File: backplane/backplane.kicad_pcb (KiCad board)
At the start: 2 copper layers, 150 x 150 mm, 16 parts

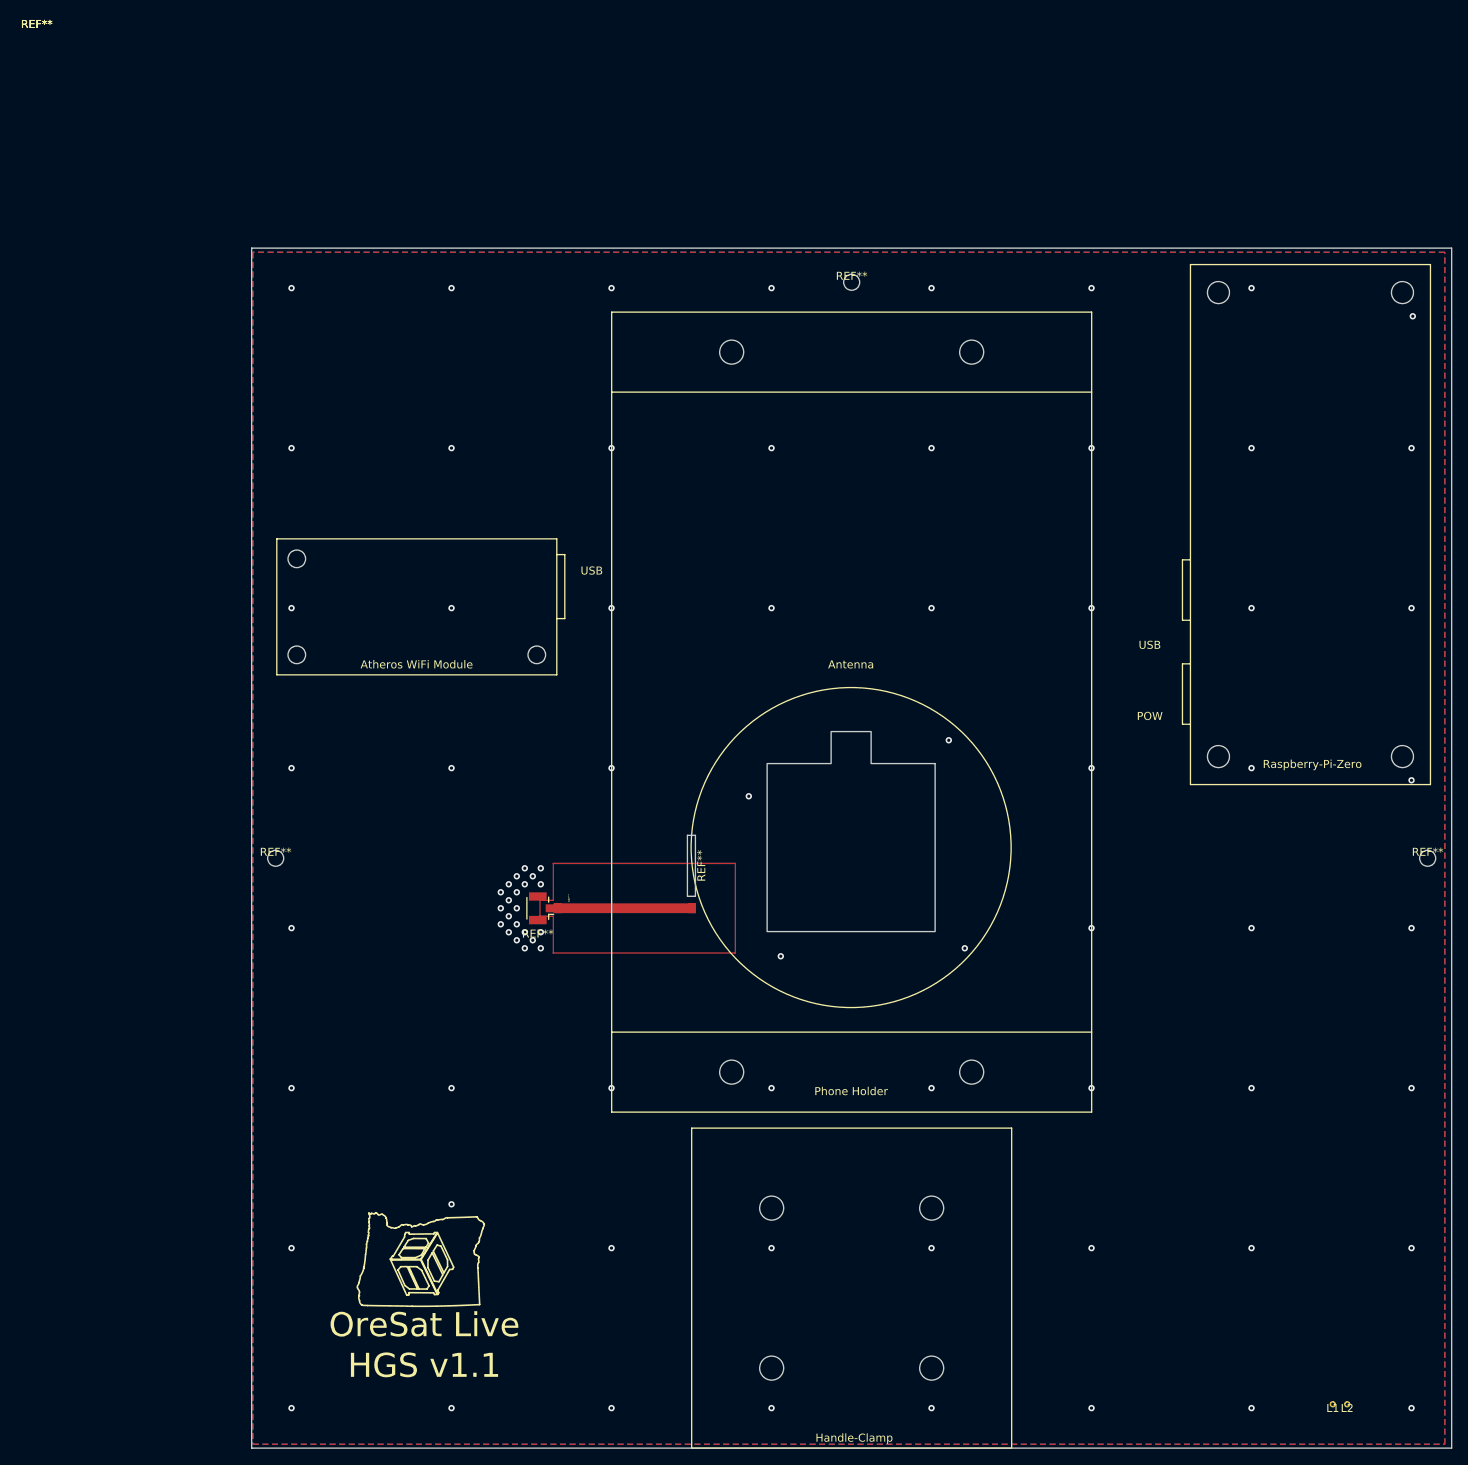
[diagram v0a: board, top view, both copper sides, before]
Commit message: Changed antenna feed slot width to be 1.5mm and other
Cleaned up floating unnecessary silkscreen
Removed solder mask for mounting holes
Updated version number text for HGS
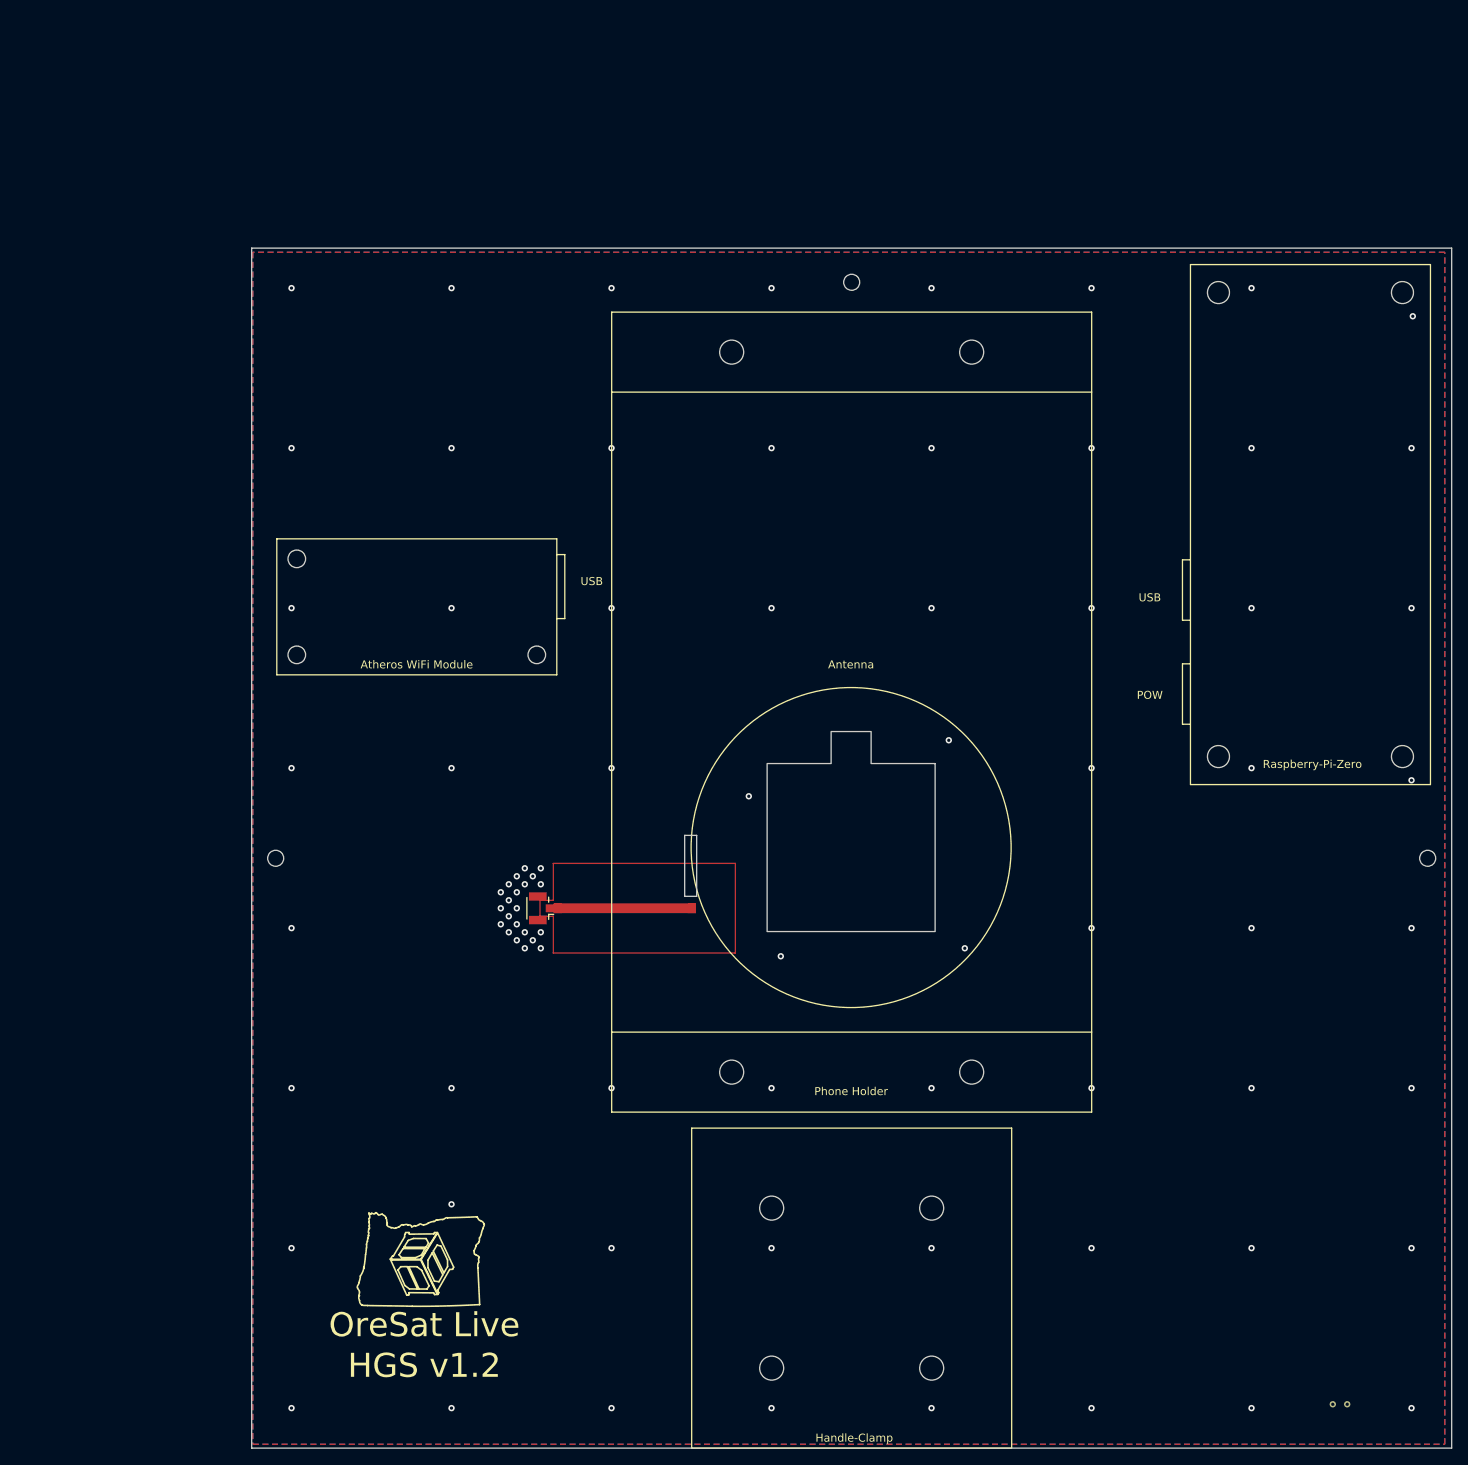
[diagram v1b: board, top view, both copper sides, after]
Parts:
- moved REF** 0.16 mm to (79.8, 107.7)

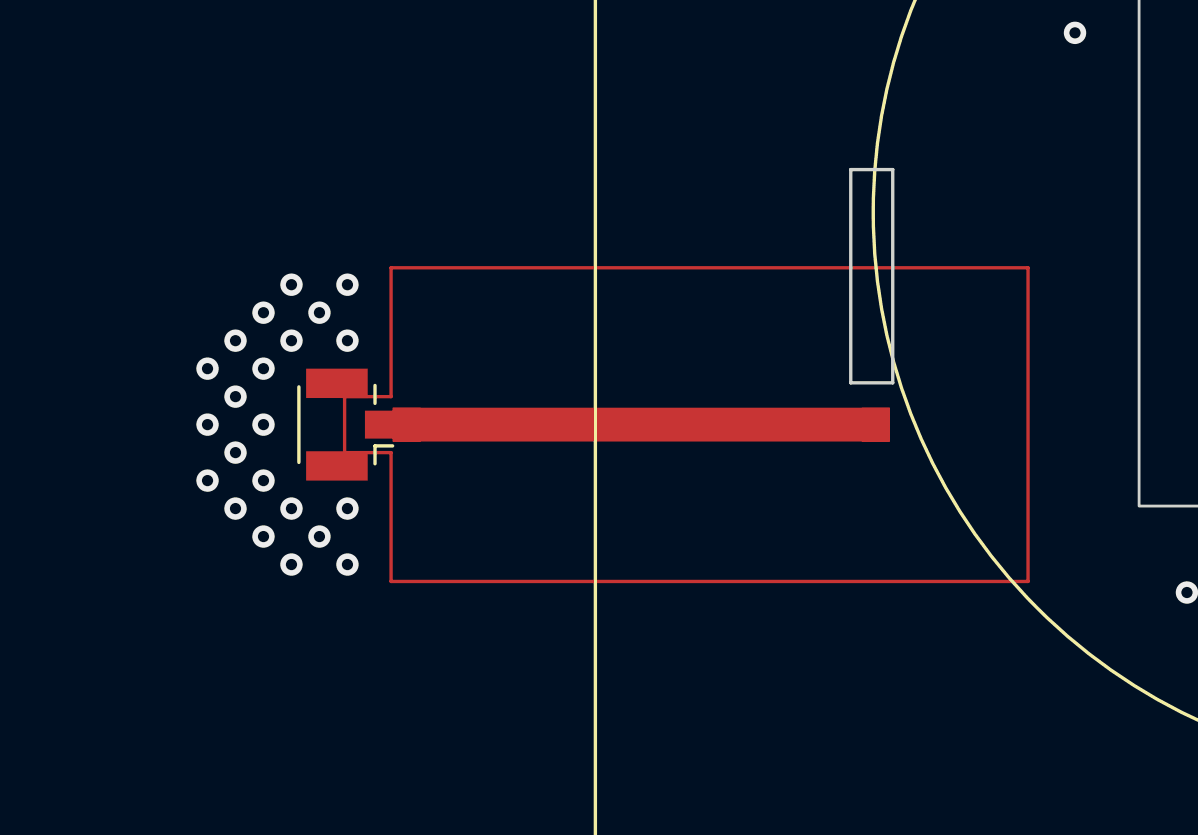
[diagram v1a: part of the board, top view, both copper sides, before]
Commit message: Shifted transformer 1mm to the side and 3mm downward
Transformer was moved so that there is a smoother transition for the
antenna wire to feed to the back of the board.
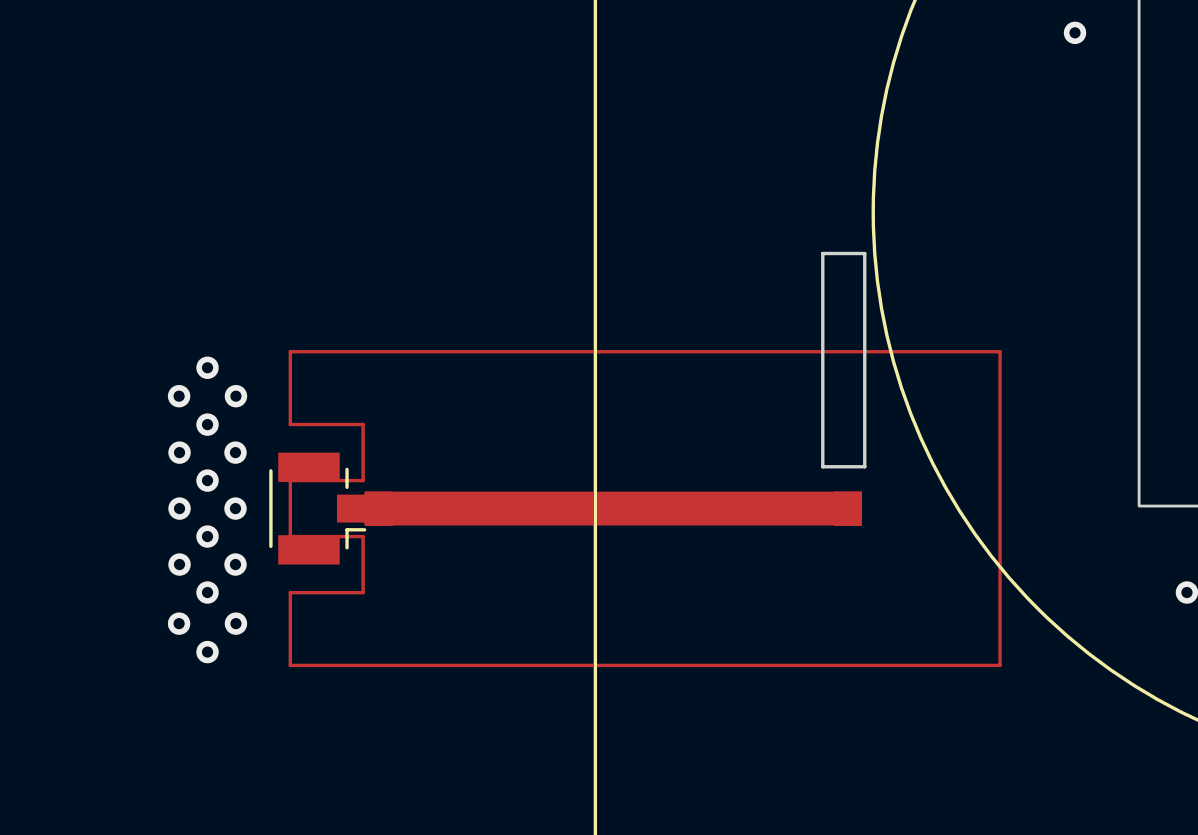
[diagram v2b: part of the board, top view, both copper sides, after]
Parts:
- moved REF** 3.16 mm to (62.0, 116.0)
- moved REF** 3.16 mm to (78.8, 110.7)
- moved REF** 3.16 mm to (58.1, 116.0)
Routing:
- net Net-(L1-Pad1): vias 84 -> 78
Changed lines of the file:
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@@
     (thickness 1.6)
     (drawings 4)
-    (tracks 84)
+    (tracks 78)
     (zones 0)
     (modules 16)
@@
     (add_net "Net-(L1-Pad1)")
   )
+  (module muwave_stub locked (layer F.Cu)
+    (at 62.03385 116 270)
+    (fp_text reference REF** (at -1.27 0.5 90) (layer B.Fab) hide
+      (effects (font (size 0.25 0.25) (thickness 0.05)))
+    )
+    (fp_text value muwave_stub (at 0 -0.5 90) (layer F.Fab)
+      (effects (font (size 0.25 0.25) (thickness 0.05)))
+    )
+    (fp_line (start -3.00469 2.475001) (end -3.00469 5.075001) (layer F.Cu) (width 0.12))
+    (fp_line (start 1 2.475001) (end 1 5.075001) (layer F.Cu) (width 0.12))
+    (fp_line (start -1 5.075001) (end 1 5.075001) (layer F.Cu) (width 0.12))
+    (fp_line (start -5.60469 5.075001) (end -3.00469 5.075001) (layer F.Cu) (width 0.12))
+    (fp_line (start -5.60469 -20.287299) (end 5.60469 -20.287299) (layer F.Cu) (width 0.12))
+    (fp_line (start -5.60469 -20.287299) (end -5.60469 5.075001) (layer F.Cu) (width 0.12))
+    (fp_line (start -1 2.475001) (end -1 5.075001) (layer F.Cu) (width 0.12))
+    (fp_line (start -3.00469 2.475001) (end -1 2.475001) (layer F.Cu) (width 0.12))
+    (fp_line (start 3.00469 2.475001) (end 1 2.475001) (layer F.Cu) (width 0.12))
+    (fp_line (start 5.60469 -20.287299) (end 5.60469 5.075001) (layer F.Cu) (width 0.12))
+    (fp_line (start 5.60469 5.075001) (end 3.00469 5.075001) (layer F.Cu) (width 0.12))
+    (fp_line (start 3.00469 2.475001) (end 3.00469 5.075001) (layer F.Cu) (width 0.12))
+    (pad 1 smd rect (at 0 -6.46615 270) (size 1.20938 17.7623) (layers F.Cu))
+    (pad 1 smd rect (at 0 -14.8473 270) (size 1.20938 1) (layers F.Cu F.Mask))
+    (pad 1 smd rect (at 0 1.915 270) (size 1.20938 1) (layers F.Cu F.Mask))
+  )
   (module DxWiFi:antenna-wire-slot (layer F.Cu)
-    (at 79.756 107.696 270)
+    (at 78.756 110.696 270)
     (fp_text reference REF** (at 0 0.5 270) (layer B.Fab) hide
       (effects (font (size 1 1) (thickness 0.15)))
@@
   )
   (module Connector_Coaxial:U.FL_Hirose_U.FL-R-SMT-1_Vertical (layer F.Cu)
-    (at 59.1 113 180)
+    (at 58.1 116 180)
     (descr "Hirose U.FL Coaxial https://www.hirose.com/product/en/products/U.FL/U.FL-R-SMT-1%2810%29/")
     (tags "Hirose U.FL Coaxial")
@@
     (pad "" np_thru_hole circle (at 10 -10) (size 3 3) (drill 3) (layers *.Cu))
   )
-  (module muwave_stub locked (layer F.Cu)
-    (at 63.03385 113 270)
-    (fp_text reference REF** (at -1.27 0.5 270) (layer B.Fab) hide
-      (effects (font (size 0.25 0.25) (thickness 0.05)))
-    )
-    (fp_text value muwave_stub (at 0 -0.5 270) (layer F.Fab)
-      (effects (font (size 0.25 0.25) (thickness 0.05)))
-    )
-    (fp_line (start -1 2.475001) (end -1 4.135001) (layer F.Cu) (width 0.12))
-    (fp_line (start 1 2.475001) (end 5.60469 2.475001) (layer F.Cu) (width 0.12))
-    (fp_line (start -5.60469 -20.287299) (end -5.60469 2.475001) (layer F.Cu) (width 0.12))
-    (fp_line (start -5.60469 -20.287299) (end 5.60469 -20.287299) (layer F.Cu) (width 0.12))
-    (fp_line (start 5.60469 -20.287299) (end 5.60469 2.475001) (layer F.Cu) (width 0.12))
-    (fp_line (start -5.60469 2.475001) (end -1 2.475001) (layer F.Cu) (width 0.12))
-    (fp_line (start 1 2.475001) (end 1 4.135001) (layer F.Cu) (width 0.12))
-    (fp_line (start -1 4.135001) (end 1 4.135001) (layer F.Cu) (width 0.12))
-    (pad 1 smd rect (at 0 1.915 270) (size 1.20938 1) (layers F.Cu F.Mask))
-    (pad 1 smd rect (at 0 -14.8473 270) (size 1.20938 1) (layers F.Cu F.Mask))
-    (pad 1 smd rect (at 0 -6.46615 270) (size 1.20938 17.7623) (layers F.Cu))
-  )
   (gr_line (start 22.86 180.48) (end 22.86 30.48) (layer Edge.Cuts) (width 0.05))
   (gr_line (start 172.86 180.48) (end 22.86 180.48) (layer Edge.Cuts) (width 0.05))
   (gr_line (start 172.86 30.48) (end 172.86 180.48) (layer Edge.Cuts) (width 0.05))
   (gr_line (start 22.86 30.48) (end 172.86 30.48) (layer Edge.Cuts) (width 0.05))
-  (via (at 59 110) (size 0.8) (drill 0.4) (layers F.Cu B.Cu) (net 1))
-  (via (at 59 108) (size 0.8) (drill 0.4) (layers F.Cu B.Cu) (net 1))
-  (via (at 58 109) (size 0.8) (drill 0.4) (layers F.Cu B.Cu) (net 1))
-  (via (at 57 108) (size 0.8) (drill 0.4) (layers F.Cu B.Cu) (net 1))
-  (via (at 57 110) (size 0.8) (drill 0.4) (layers F.Cu B.Cu) (net 1))
-  (via (at 56 109) (size 0.8) (drill 0.4) (layers F.Cu B.Cu) (net 1))
-  (via (at 56 111) (size 0.8) (drill 0.4) (layers F.Cu B.Cu) (net 1))
-  (via (at 55 112) (size 0.8) (drill 0.4) (layers F.Cu B.Cu) (net 1))
-  (via (at 56 113) (size 0.8) (drill 0.4) (layers F.Cu B.Cu) (net 1))
+  (via (at 52.984 111.984) (size 0.8) (drill 0.4) (layers F.Cu B.Cu) (net 1))
+  (via (at 55.016 111.984) (size 0.8) (drill 0.4) (layers F.Cu B.Cu) (net 1))
+  (via (at 54 110.968) (size 0.8) (drill 0.4) (layers F.Cu B.Cu) (net 1))
+  (via (at 55.016 120.112) (size 0.8) (drill 0.4) (layers F.Cu B.Cu) (net 1))
+  (via (at 52.984 120.112) (size 0.8) (drill 0.4) (layers F.Cu B.Cu) (net 1))
+  (via (at 54 121.128) (size 0.8) (drill 0.4) (layers F.Cu B.Cu) (net 1))
   (via (at 55 114) (size 0.8) (drill 0.4) (layers F.Cu B.Cu) (net 1))
-  (via (at 56 115) (size 0.8) (drill 0.4) (layers F.Cu B.Cu) (net 1))
+  (via (at 54 115) (size 0.8) (drill 0.4) (layers F.Cu B.Cu) (net 1))
   (via (at 55 116) (size 0.8) (drill 0.4) (layers F.Cu B.Cu) (net 1))
-  (via (at 56 117) (size 0.8) (drill 0.4) (layers F.Cu B.Cu) (net 1))
-  (via (at 57 116) (size 0.8) (drill 0.4) (layers F.Cu B.Cu) (net 1))
-  (via (at 58 117) (size 0.8) (drill 0.4) (layers F.Cu B.Cu) (net 1))
-  (via (at 59 116) (size 0.8) (drill 0.4) (layers F.Cu B.Cu) (net 1))
-  (via (at 59 118) (size 0.8) (drill 0.4) (layers F.Cu B.Cu) (net 1))
-  (via (at 57 118) (size 0.8) (drill 0.4) (layers F.Cu B.Cu) (net 1))
-  (via (at 54 111) (size 0.8) (drill 0.4) (layers F.Cu B.Cu) (net 1))
+  (via (at 54 117) (size 0.8) (drill 0.4) (layers F.Cu B.Cu) (net 1))
+  (via (at 55 118) (size 0.8) (drill 0.4) (layers F.Cu B.Cu) (net 1))
+  (via (at 54 119) (size 0.8) (drill 0.4) (layers F.Cu B.Cu) (net 1))
+  (via (at 53 114) (size 0.8) (drill 0.4) (layers F.Cu B.Cu) (net 1))
+  (via (at 53 116) (size 0.8) (drill 0.4) (layers F.Cu B.Cu) (net 1))
+  (via (at 53 118) (size 0.8) (drill 0.4) (layers F.Cu B.Cu) (net 1))
   (via (at 54 113) (size 0.8) (drill 0.4) (layers F.Cu B.Cu) (net 1))
-  (via (at 54 115) (size 0.8) (drill 0.4) (layers F.Cu B.Cu) (net 1))
-  (via (at 55 110) (size 0.8) (drill 0.4) (layers F.Cu B.Cu) (net 1))
   (via (at 167.84 175.48) (size 0.8) (drill 0.4) (layers F.Cu B.Cu) (net 1))
   (via (at 147.84 175.48) (size 0.8) (drill 0.4) (layers F.Cu B.Cu) (net 1))
